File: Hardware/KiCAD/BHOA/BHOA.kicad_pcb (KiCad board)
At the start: 4 copper layers, 100 x 100 mm, 148 parts, among them J1 Bal Input, J10 Input SW L, J11 UnBal Input, J12 Input SW R, J2 Prestage SW R, J4 PWR, J5 Prestage SW L, J6 Output Stage Out, J8 SW Conn, J9 SW Conn, U100 OPA1688, U101 OPA1688, U102 OPA1688, U103 OPA1688, U200 OPA1688, U201 OPA1688, U202 OPA1688, U203 OPA1688, U300 OPA1688, U301 OPA1688, U302 OPA1688, U303 OPA1688, U400 OPA1688, U401 OPA1688, U402 OPA1688, U403 OPA1688, U601 OPA1688, U602 LME49724, U701 OPA1688, U702 LME49724

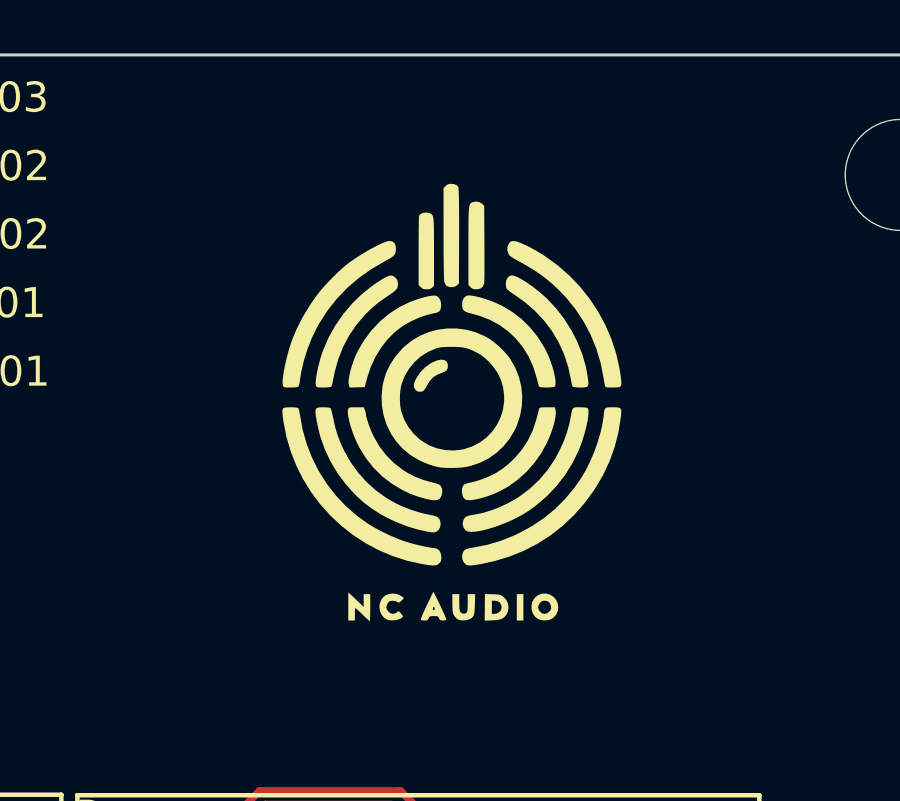
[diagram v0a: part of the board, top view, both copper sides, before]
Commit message: changed logo to c audio
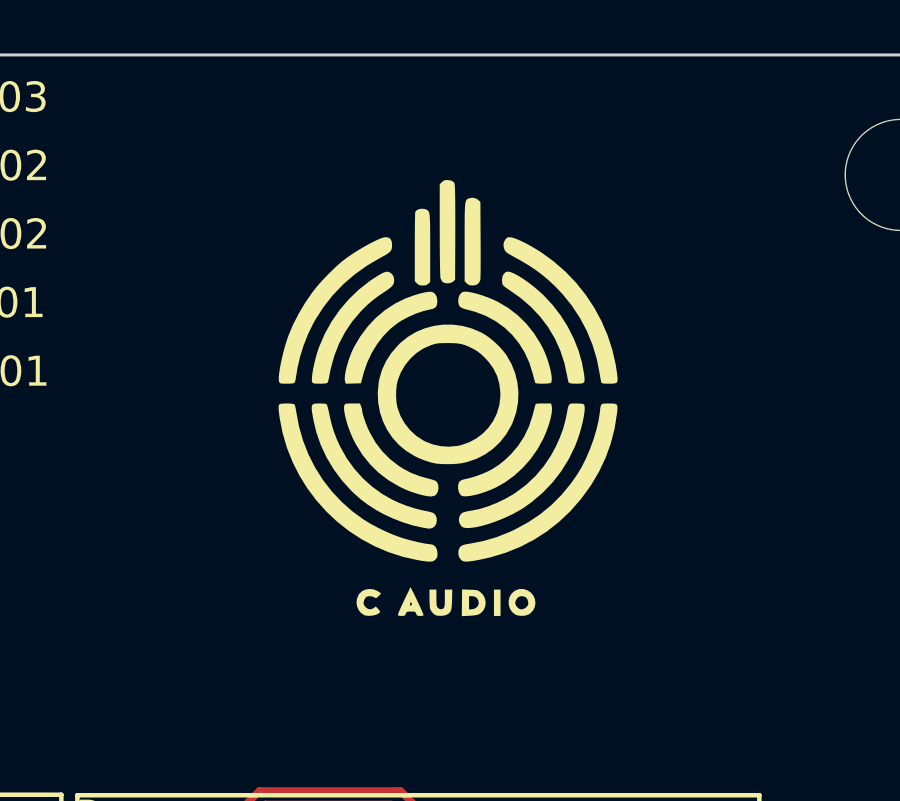
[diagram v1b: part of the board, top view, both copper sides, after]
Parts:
- removed the G*** at (181.1, 60.5)
- added G***: LOGO, Logos:C Audio Logo 25mm, F.Cu at (181.0, 60.3)

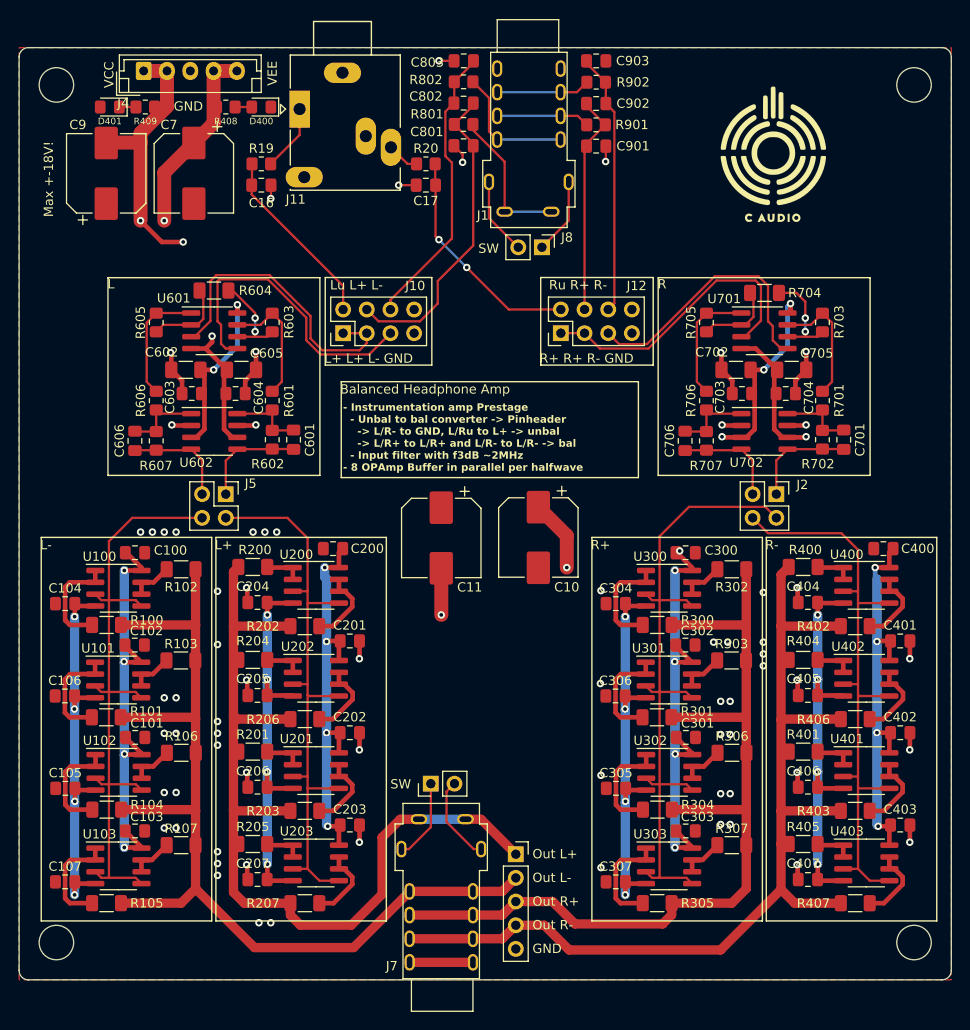
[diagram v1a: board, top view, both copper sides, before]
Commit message: Updated PCB with output protection
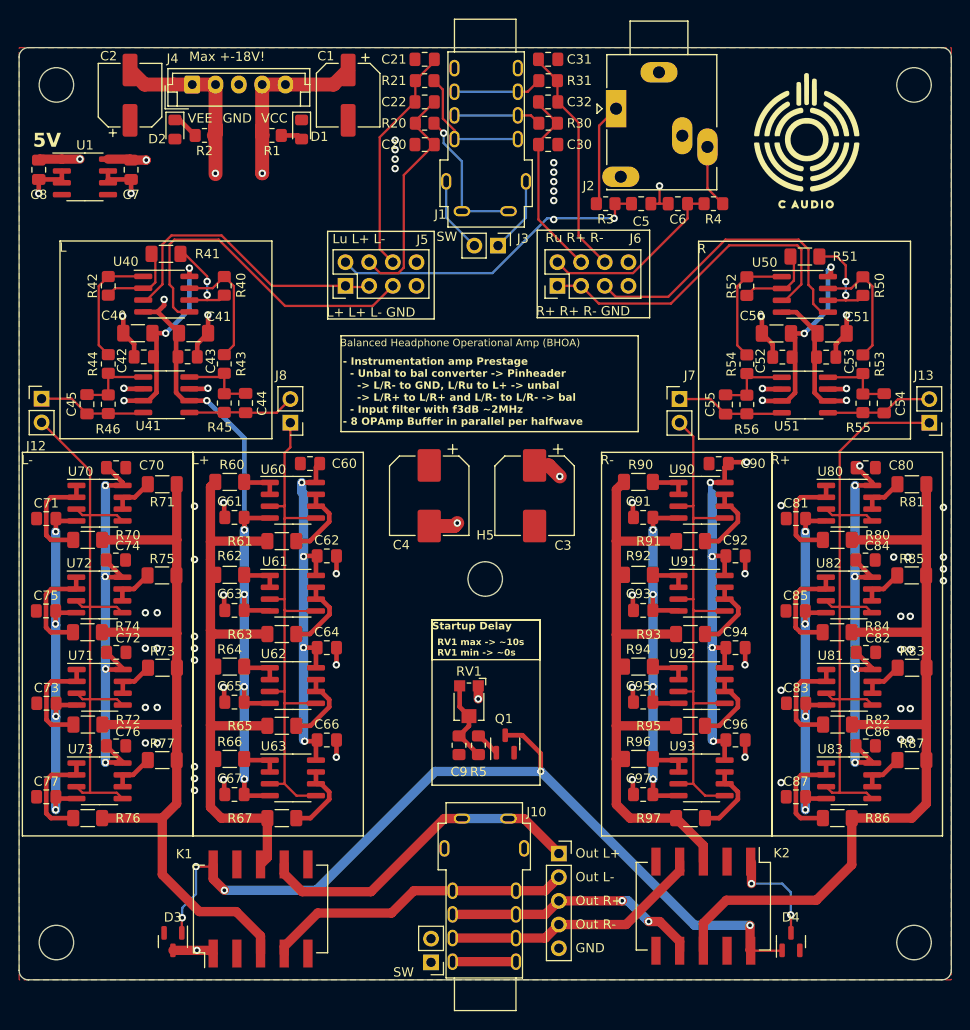
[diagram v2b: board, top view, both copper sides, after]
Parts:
- removed D400, D401: Grn, LED_SMD:LED_0805_2012Metric_Pad1.15x1.40mm_HandSolder
- removed the J10 at (134.8, 79.6)
- removed the J2 at (181.2, 96.9)
- removed R408, R409: 4k7, Resistor_SMD:R_0805_2012Metric_Pad1.20x1.40mm_HandSolder
- added C2: 47u, Capacitor_SMD:CP_Elec_6.3x5.8, F.Cu at (111.9, 54.1)
- added C7: 1u, Capacitor_SMD:C_0805_2012Metric_Pad1.18x1.45mm_HandSolder, F.Cu at (112.0, 62.1)
- added C8: 1u, Capacitor_SMD:C_0805_2012Metric_Pad1.18x1.45mm_HandSolder, F.Cu at (102.1, 62.1)
- added D1: Grn, LED_SMD:LED_0805_2012Metric_Pad1.15x1.40mm_HandSolder, F.Cu at (130.3, 57.8)
- added D2: Grn, LED_SMD:LED_0805_2012Metric_Pad1.15x1.40mm_HandSolder, F.Cu at (116.7, 57.8)
- added D3: BAS21, Package_TO_SOT_SMD:SOT-23, F.Cu at (116.5, 144.9)
- added D4: BAS21, Package_TO_SOT_SMD:SOT-23, F.Cu at (182.8, 144.9)
- added H5: MountingHole, MountingHole:MountingHole_3.7mm, F.Cu at (150.0, 106.0)
- added J13: Out_R+, Connector_PinHeader_2.54mm:PinHeader_1x02_P2.54mm_Vertical, F.Cu at (197.6, 89.2)
- added J6: Input SW R, Connector_PinHeader_2.54mm:PinHeader_2x04_P2.54mm_Vertical, F.Cu at (157.7, 74.6)
- added J7: Out_R-, Connector_PinHeader_2.54mm:PinHeader_1x02_P2.54mm_Vertical, F.Cu at (170.8, 86.7)
- added J8: Out_L+, Connector_PinHeader_2.54mm:PinHeader_1x02_P2.54mm_Vertical, F.Cu at (129.1, 89.2)
- added K1: EB2-5NU, Relay_SMD:Relay_DPDT_FRT5_SMD, F.Cu at (125.9, 141.4)
- added K2: EB2-5NU, Relay_SMD:Relay_DPDT_FRT5_SMD, F.Cu at (173.4, 141.1)
- added Q1: 2N7002K, Package_TO_SOT_SMD:SOT-23, F.Cu at (152.1, 123.7)
- added R1: 4k7, Resistor_SMD:R_0805_2012Metric_Pad1.20x1.40mm_HandSolder, F.Cu at (127.1, 58.4)
- added R2: 4k7, Resistor_SMD:R_0805_2012Metric_Pad1.20x1.40mm_HandSolder, F.Cu at (119.9, 58.4)
- added R5: 200R, Resistor_SMD:R_0805_2012Metric_Pad1.20x1.40mm_HandSolder, F.Cu at (149.3, 123.8)
- added RV1: 50k, Potentiometer_SMD:Potentiometer_Bourns_TC33X_Vertical, F.Cu at (148.3, 119.3)
- added U1: L78L05_SO8, Package_SO:SOIC-8_3.9x4.9mm_P1.27mm, F.Cu at (107.1, 62.9)
- C1: renamed from C7; value 220u -> 47u; footprint Capacitor_SMD:CP_Elec_8x10 -> Capacitor_SMD:CP_Elec_6.3x5.8
- C9: value 220u -> 100u; footprint Capacitor_SMD:CP_Elec_8x10 -> Resistor_SMD:R_0805_2012Metric_Pad1.20x1.40mm_HandSolder
- J12: value Input SW R -> Out_L-; footprint Connector_PinHeader_2.54mm:PinHeader_2x04_P2.54mm_Vertical -> Connector_PinHeader_2.54mm:PinHeader_1x02_P2.54mm_Vertical
- J5: value Prestage SW L -> Input SW L; footprint Connector_PinHeader_2.54mm:PinHeader_2x02_P2.54mm_Vertical -> Connector_PinHeader_2.54mm:PinHeader_2x04_P2.54mm_Vertical
- moved C9 72.1 mm to (147.2, 123.8), turned to -90 degrees
- moved J12 56.1 mm to (102.4, 86.7), turned to 0 degrees
- moved C5 40.8 mm to (166.7, 65.7)
- moved R3 37.2 mm to (162.9, 65.7), turned to 0 degrees
- moved J2 34.0 mm to (164.0, 55.5)
- moved R4 31.1 mm to (174.5, 65.7), turned to 180 degrees
- moved C6 27.1 mm to (170.7, 65.7)
- moved J5 25.8 mm to (135.0, 74.6), turned to 90 degrees
- moved C87 21.4 mm to (183.3, 129.4)
- moved R86 21.4 mm to (187.8, 131.7)
- moved C80 21.4 mm to (190.8, 94.1)
- moved R80 21.4 mm to (187.8, 101.8)
- moved R81 21.4 mm to (195.8, 95.8)
- moved R83 21.4 mm to (195.8, 115.5)
- moved R87 21.4 mm to (195.8, 125.4)
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- renumbered C801 to C20, C803 to C21, C802 to C22, C10 to C3, C901 to C30, C903 to C31, C902 to C32, C11 to C4, C602 to C40, C605 to C41, C603 to C42, C604 to C43, C601 to C44, C606 to C45, C16 to C5, C702 to C50, C705 to C51, C703 to C52, C704 to C53, C701 to C54, C706 to C55, C17 to C6, C200 to C60, C204 to C61, C201 to C62, C205 to C63, C202 to C64, C206 to C65, C203 to C66, C207 to C67, C100 to C70, C104 to C71, C101 to C72, C105 to C73, C102 to C74, C106 to C75, C103 to C76, C107 to C77, C300 to C80, C304 to C81, C301 to C82, C305 to C83, C302 to C84, C306 to C85, C303 to C86, C307 to C87, C400 to C90, C404 to C91, C401 to C92, C405 to C93, C402 to C94, C406 to C95, C403 to C96, C407 to C97, H101 to H1, H102 to H2, H103 to H3, H104 to H4, J7 to J10, J6 to J11, J11 to J2, J8 to J3, R801 to R20, R802 to R21, R19 to R3, R901 to R30, R902 to R31, R20 to R4, R603 to R40, R604 to R41, R605 to R42, R601 to R43, R606 to R44, R602 to R45, R607 to R46, R703 to R50, R704 to R51, R705 to R52, R701 to R53, R706 to R54, R702 to R55, R707 to R56, R200 to R60, R202 to R61, R204 to R62, R206 to R63, R201 to R64, R203 to R65, R205 to R66, R207 to R67, R100 to R70, R102 to R71, R104 to R72, R106 to R73, R101 to R74, R103 to R75, R105 to R76, R107 to R77, R300 to R80, R302 to R81, R304 to R82, R306 to R83, R301 to R84, R303 to R85, R305 to R86, R307 to R87, R400 to R90, R402 to R91, R404 to R92, R406 to R93, R401 to R94, R403 to R95, R405 to R96, R407 to R97, U601 to U40, U602 to U41, U701 to U50, U702 to U51, U200 to U60, U202 to U61, U201 to U62, U203 to U63, U100 to U70, U102 to U71, U101 to U72, U103 to U73, U300 to U80, U302 to U81, U301 to U82, U303 to U83, U400 to U90, U402 to U91, U401 to U92, U403 to U93
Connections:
- C9 pad 1: GND -> Net-(C9-Pad1)
- C9 pad 2: VEE -> GND
- J12 pad 1: /In_pre_R_+ -> /Out_pre_L_-
- J12 pad 2: /In_R_unbal_filtered -> /In_out_L_-
- J5 pad 1: /Out_pre_L_+ -> /In_pre_L_+
- J5 pad 2: /In_out_L_+ -> /In_L_unbal_filtered
- J5 pad 3: /Out_pre_L_- -> /In_pre_L_+
- J5 pad 4: /In_out_L_- -> /In_L+_bal_filtered
- R60 pad 2: /Out_L_+ -> /Amplifier L+/Out
- R61 pad 2: /Out_L_+ -> /Amplifier L+/Out
- R62 pad 2: /Out_L_+ -> /Amplifier L+/Out
- R63 pad 2: /Out_L_+ -> /Amplifier L+/Out
- R64 pad 2: /Out_L_+ -> /Amplifier L+/Out
- R65 pad 2: /Out_L_+ -> /Amplifier L+/Out
- R66 pad 2: /Out_L_+ -> /Amplifier L+/Out
- R67 pad 2: /Out_L_+ -> /Amplifier L+/Out
- R70 pad 2: /Out_L_- -> /Amplifier L-/Out
- R71 pad 2: /Out_L_- -> /Amplifier L-/Out
- R72 pad 2: /Out_L_- -> /Amplifier L-/Out
- R73 pad 2: /Out_L_- -> /Amplifier L-/Out
- R74 pad 2: /Out_L_- -> /Amplifier L-/Out
- R75 pad 2: /Out_L_- -> /Amplifier L-/Out
- R76 pad 2: /Out_L_- -> /Amplifier L-/Out
- R77 pad 2: /Out_L_- -> /Amplifier L-/Out
- R80 pad 2: /Out_R_+ -> /Amplifier R+/Out
- R81 pad 2: /Out_R_+ -> /Amplifier R+/Out
- R82 pad 2: /Out_R_+ -> /Amplifier R+/Out
- R83 pad 2: /Out_R_+ -> /Amplifier R+/Out
- R84 pad 2: /Out_R_+ -> /Amplifier R+/Out
- R85 pad 2: /Out_R_+ -> /Amplifier R+/Out
- R86 pad 2: /Out_R_+ -> /Amplifier R+/Out
- R87 pad 2: /Out_R_+ -> /Amplifier R+/Out
- R90 pad 2: /Out_R_- -> /Amplifier R-/Out
- R91 pad 2: /Out_R_- -> /Amplifier R-/Out
- R92 pad 2: /Out_R_- -> /Amplifier R-/Out
- R93 pad 2: /Out_R_- -> /Amplifier R-/Out
- R94 pad 2: /Out_R_- -> /Amplifier R-/Out
- R95 pad 2: /Out_R_- -> /Amplifier R-/Out
- R96 pad 2: /Out_R_- -> /Amplifier R-/Out
- R97 pad 2: /Out_R_- -> /Amplifier R-/Out
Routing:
- net +5V: track 0.00 -> 130.0 mm, vias 0 -> 5
- net /r_mute: track 0.00 -> 94.2 mm, vias 0 -> 5
- net /Amplifier R+/Out: track 0.00 -> 93.5 mm
- net /Amplifier L-/Out: track 0.00 -> 88.2 mm
- net /Out_R_-: track 106.3 -> 28.3 mm
- net /Out_L_-: track 107.1 -> 33.3 mm
- net /Out_R_+: track 98.4 -> 27.8 mm, vias 0 -> 2
- net /Amplifier R-/Out: track 0.00 -> 67.9 mm
- net /Amplifier L+/Out: track 0.00 -> 65.5 mm
- net /Out_L_+: track 96.0 -> 36.1 mm
- net VEE: track 359.2 -> 324.0 mm
- net VCC: track 360.0 -> 325.8 mm, vias 24 -> 27
- net /In_L_unbal_filtered: track 19.7 -> 35.2 mm, vias 0 -> 2
- net Net-(C9-Pad1): track 0.00 -> 9.14 mm
- net /In_L+_bal_filtered: track 33.7 -> 25.3 mm
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- added copper zone on In2.Cu, net +5V
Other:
- board text added: "5V"
- board text added: "Balanced Headphone Operational Amp (BHOA)"
- board text added: "RV1 max -> ~10s RV1 min -> ~0s"
- board text added: "Startup Delay"
- board text removed: "Balanced Headphone Amp"

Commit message: housekeeping
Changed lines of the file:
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@@
       (drillshape 0)
       (scaleselection 1)
-      (outputdirectory "production/bal_headamp_OP_gerbers/")
+      (outputdirectory "../../production/C Audio BHOA_gerbers/")
     )
   )
@@
     (fp_line (start 1 0.625) (end -1 0.625)
       (stroke (width 0.1) (type solid)) (layer "F.Fab"))
-    (pad "1" smd roundrect (at -1 0 270) (size 1.2 1.4) (layers "F.Cu" "F.Paste" "F.Mask") (roundrect_rratio 0.208333)
+    (pad "1" smd roundrect (at -1 0 270) (size 1.2 1.4) (layers "F.Cu" "F.Paste" "F.Mask") (roundrect_rratio 0.2083333333)
       (net 5 "Net-(C9-Pad1)") (pintype "passive"))
-    (pad "2" smd roundrect (at 1 0 270) (size 1.2 1.4) (layers "F.Cu" "F.Paste" "F.Mask") (roundrect_rratio 0.208333)
+    (pad "2" smd roundrect (at 1 0 270) (size 1.2 1.4) (layers "F.Cu" "F.Paste" "F.Mask") (roundrect_rratio 0.2083333333)
       (net 2 "GND") (pintype "passive"))
     (model "${KICAD6_3DMODEL_DIR}/Resistor_SMD.3dshapes/R_0805_2012Metric.wrl"
@@
     (fp_line (start 1 0.625) (end -1 0.625)
       (stroke (width 0.1) (type solid)) (layer "F.Fab"))
-    (pad "1" smd roundrect (at -1.0375 0 270) (size 1.175 1.45) (layers "F.Cu" "F.Paste" "F.Mask") (roundrect_rratio 0.212766)
+    (pad "1" smd roundrect (at -1.0375 0 270) (size 1.175 1.45) (layers "F.Cu" "F.Paste" "F.Mask") (roundrect_rratio 0.2127659574)
       (net 1 "VCC") (pintype "passive"))
-    (pad "2" smd roundrect (at 1.0375 0 270) (size 1.175 1.45) (layers "F.Cu" "F.Paste" "F.Mask") (roundrect_rratio 0.212766)
+    (pad "2" smd roundrect (at 1.0375 0 270) (size 1.175 1.45) (layers "F.Cu" "F.Paste" "F.Mask") (roundrect_rratio 0.2127659574)
       (net 2 "GND") (pintype "passive"))
     (model "${KICAD6_3DMODEL_DIR}/Capacitor_SMD.3dshapes/C_0805_2012Metric.wrl"
@@
     (fp_line (start 1 0.625) (end -1 0.625)
       (stroke (width 0.1) (type solid)) (layer "F.Fab"))
-    (pad "1" smd roundrect (at -1 0) (size 1.2 1.4) (layers "F.Cu" "F.Paste" "F.Mask") (roundrect_rratio 0.208333)
+    (pad "1" smd roundrect (at -1 0) (size 1.2 1.4) (layers "F.Cu" "F.Paste" "F.Mask") (roundrect_rratio 0.2083333333)
       (net 1 "VCC") (pintype "passive"))
-    (pad "2" smd roundrect (at 1 0) (size 1.2 1.4) (layers "F.Cu" "F.Paste" "F.Mask") (roundrect_rratio 0.208333)
+    (pad "2" smd roundrect (at 1 0) (size 1.2 1.4) (layers "F.Cu" "F.Paste" "F.Mask") (roundrect_rratio 0.2083333333)
       (net 6 "Net-(D1-A)") (pintype "passive"))
     (model "${KICAD6_3DMODEL_DIR}/Resistor_SMD.3dshapes/R_0805_2012Metric.wrl"
@@
     (fp_line (start 1 0.625) (end -1 0.625)
       (stroke (width 0.1) (type solid)) (layer "F.Fab"))
-    (pad "1" smd roundrect (at -1 0 180) (size 1.2 1.4) (layers "F.Cu" "F.Paste" "F.Mask") (roundrect_rratio 0.208333)
+    (pad "1" smd roundrect (at -1 0 180) (size 1.2 1.4) (layers "F.Cu" "F.Paste" "F.Mask") (roundrect_rratio 0.2083333333)
       (net 3 "VEE") (pintype "passive"))
-    (pad "2" smd roundrect (at 1 0 180) (size 1.2 1.4) (layers "F.Cu" "F.Paste" "F.Mask") (roundrect_rratio 0.208333)
+    (pad "2" smd roundrect (at 1 0 180) (size 1.2 1.4) (layers "F.Cu" "F.Paste" "F.Mask") (roundrect_rratio 0.2083333333)
       (net 99 "Net-(D2-K)") (pintype "passive"))
     (model "${KICAD6_3DMODEL_DIR}/Resistor_SMD.3dshapes/R_0805_2012Metric.wrl"
@@
     (fp_line (start 1 0.6) (end 1 -0.6)
       (stroke (width 0.1) (type solid)) (layer "F.Fab"))
-    (pad "1" smd roundrect (at -1.025 0 270) (size 1.15 1.4) (layers "F.Cu" "F.Paste" "F.Mask") (roundrect_rratio 0.217391)
+    (pad "1" smd roundrect (at -1.025 0 270) (size 1.15 1.4) (layers "F.Cu" "F.Paste" "F.Mask") (roundrect_rratio 0.2173913043)
       (net 2 "GND") (pinfunction "K") (pintype "passive"))
-    (pad "2" smd roundrect (at 1.025 0 270) (size 1.15 1.4) (layers "F.Cu" "F.Paste" "F.Mask") (roundrect_rratio 0.217391)
+    (pad "2" smd roundrect (at 1.025 0 270) (size 1.15 1.4) (layers "F.Cu" "F.Paste" "F.Mask") (roundrect_rratio 0.2173913043)
       (net 6 "Net-(D1-A)") (pinfunction "A") (pintype "passive"))
     (model "${KICAD6_3DMODEL_DIR}/LED_SMD.3dshapes/LED_0805_2012Metric.wrl"
@@
     (fp_line (start 1 0.625) (end -1 0.625)
       (stroke (width 0.1) (type solid)) (layer "F.Fab"))
-    (pad "1" smd roundrect (at -1 0 90) (size 1.2 1.4) (layers "F.Cu" "F.Paste" "F.Mask") (roundrect_rratio 0.208333)
+    (pad "1" smd roundrect (at -1 0 90) (size 1.2 1.4) (layers "F.Cu" "F.Paste" "F.Mask") (roundrect_rratio 0.2083333333)
       (net 5 "Net-(C9-Pad1)") (pintype "passive"))
-    (pad "2" smd roundrect (at 1 0 90) (size 1.2 1.4) (layers "F.Cu" "F.Paste" "F.Mask") (roundrect_rratio 0.208333)
+    (pad "2" smd roundrect (at 1 0 90) (size 1.2 1.4) (layers "F.Cu" "F.Paste" "F.Mask") (roundrect_rratio 0.2083333333)
       (net 22 "Net-(Q1-G)") (pintype "passive"))
     (model "${KICAD6_3DMODEL_DIR}/Resistor_SMD.3dshapes/R_0805_2012Metric.wrl"
@@
     (fp_line (start 1 0.6) (end 1 -0.6)
       (stroke (width 0.1) (type solid)) (layer "F.Fab"))
-    (pad "1" smd roundrect (at -1.025 0 270) (size 1.15 1.4) (layers "F.Cu" "F.Paste" "F.Mask") (roundrect_rratio 0.217391)
+    (pad "1" smd roundrect (at -1.025 0 270) (size 1.15 1.4) (layers "F.Cu" "F.Paste" "F.Mask") (roundrect_rratio 0.2173913043)
       (net 99 "Net-(D2-K)") (pinfunction "K") (pintype "passive"))
-    (pad "2" smd roundrect (at 1.025 0 270) (size 1.15 1.4) (layers "F.Cu" "F.Paste" "F.Mask") (roundrect_rratio 0.217391)
+    (pad "2" smd roundrect (at 1.025 0 270) (size 1.15 1.4) (layers "F.Cu" "F.Paste" "F.Mask") (roundrect_rratio 0.2173913043)
       (net 2 "GND") (pinfunction "A") (pintype "passive"))
     (model "${KICAD6_3DMODEL_DIR}/LED_SMD.3dshapes/LED_0805_2012Metric.wrl"
@@
     (fp_line (start 1 0.625) (end -1 0.625)
       (stroke (width 0.1) (type solid)) (layer "F.Fab"))
-    (pad "1" smd roundrect (at -1.0375 0 270) (size 1.175 1.45) (layers "F.Cu" "F.Paste" "F.Mask") (roundrect_rratio 0.212766)
+    (pad "1" smd roundrect (at -1.0375 0 270) (size 1.175 1.45) (layers "F.Cu" "F.Paste" "F.Mask") (roundrect_rratio 0.2127659574)
       (net 4 "+5V") (pintype "passive"))
-    (pad "2" smd roundrect (at 1.0375 0 270) (size 1.175 1.45) (layers "F.Cu" "F.Paste" "F.Mask") (roundrect_rratio 0.212766)
+    (pad "2" smd roundrect (at 1.0375 0 270) (size 1.175 1.45) (layers "F.Cu" "F.Paste" "F.Mask") (roundrect_rratio 0.2127659574)
       (net 2 "GND") (pintype "passive"))
     (model "${KICAD6_3DMODEL_DIR}/Capacitor_SMD.3dshapes/C_0805_2012Metric.wrl"
